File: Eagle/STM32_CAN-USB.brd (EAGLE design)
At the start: 50 x 50 mm, 52 parts, among them IC1 STM32F105RBT, IC2 TJA1055T, IC3 BD9G101G, IC4 LM1117IMPX-3.3, Q1 16MHz, X1 MINI-USB

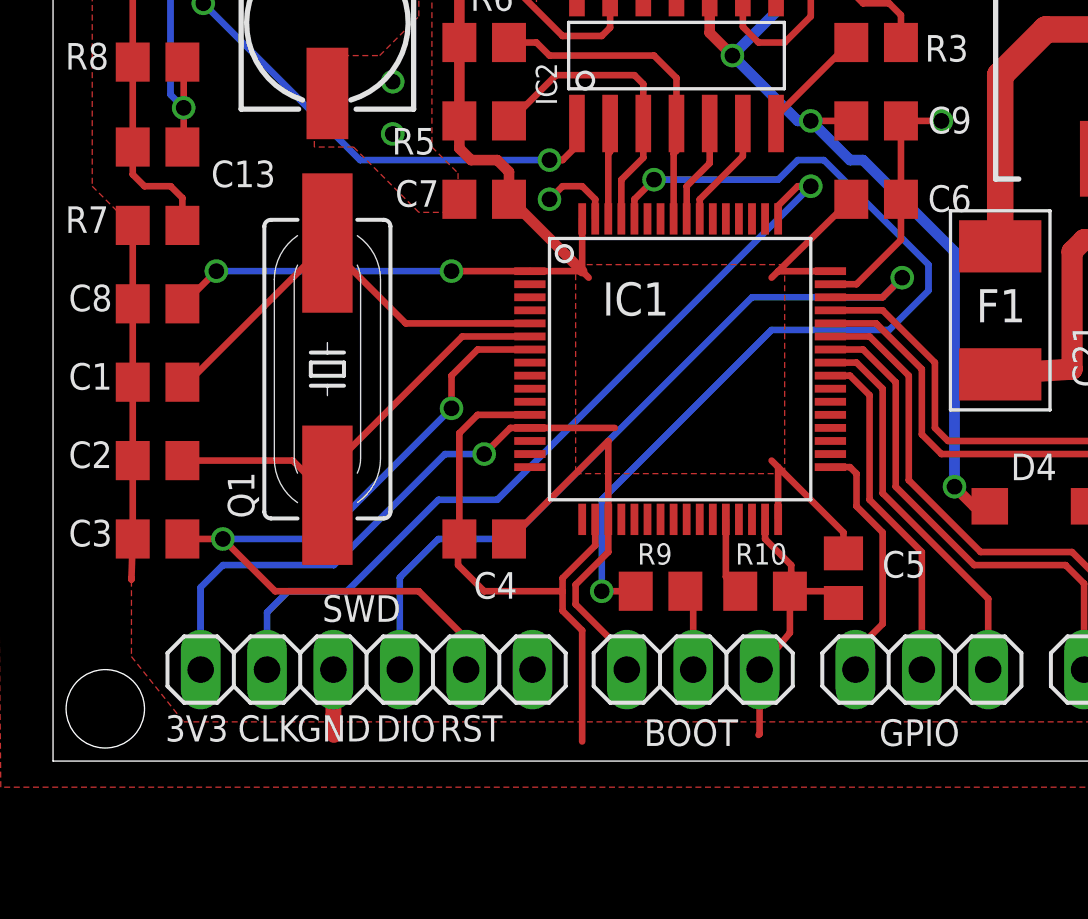
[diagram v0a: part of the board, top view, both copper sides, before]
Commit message: delete boot, edit SWD
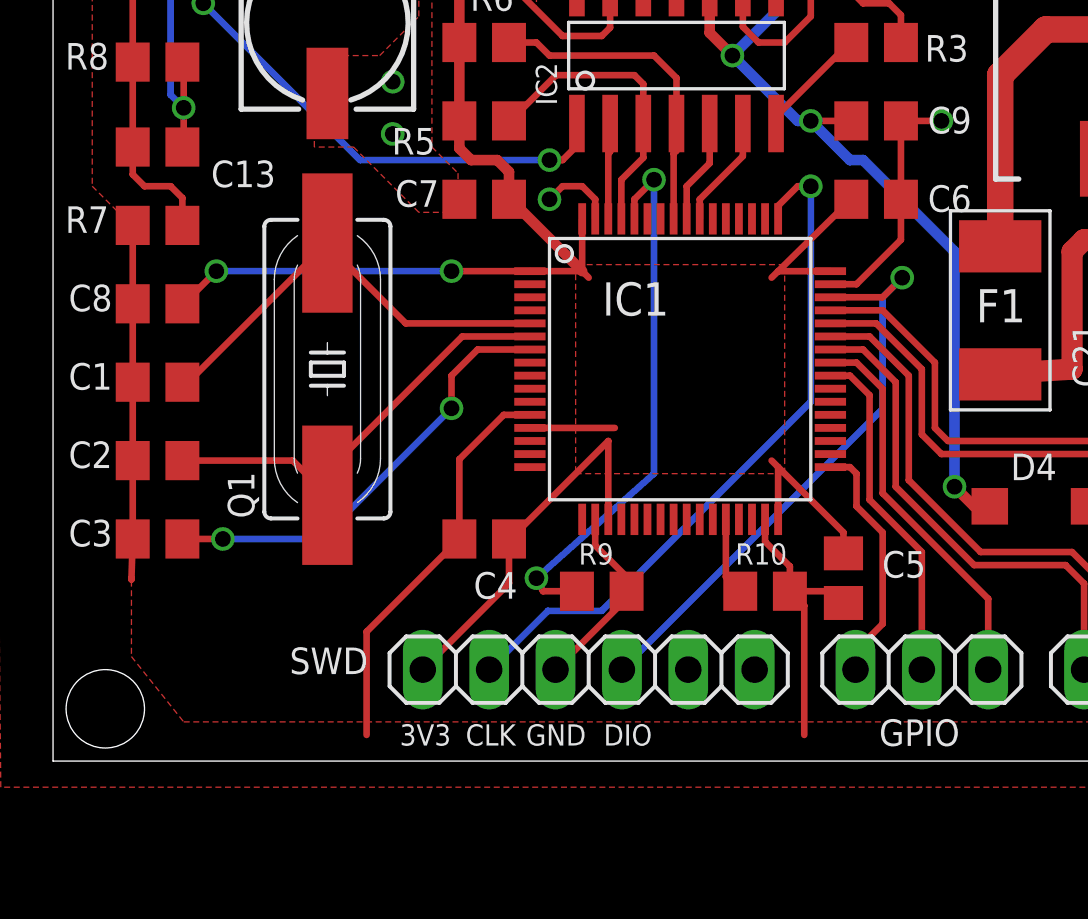
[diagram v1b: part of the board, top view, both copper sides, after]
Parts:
- removed BOOT: (no value), pinhead:1X03
- moved SWD 8.50 mm to (26.5, 8.50)
- moved R9 2.25 mm to (27.0, 11.5)
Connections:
- net BOOT0 renamed N$3
- removed net N$3 (its old number): BOOT.2, R9.2
- net +3V3: no longer BOOT.1
- net GND: now also R9.2; no longer BOOT.3
- net NRST: no longer SWD.5
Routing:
- net +3V3: track 125.0 -> 106.0 mm, vias 6 -> 5
- net N$3: track 35.9 -> 20.9 mm
- net NRST: track 29.1 -> 17.0 mm
- net SWDIO: track 30.6 -> 22.5 mm
- net SWCLK: track 31.8 -> 26.9 mm
- net N$3 (its old number): track 3.12 -> 0.00 mm
- net GND: track 120.1 -> 118.4 mm
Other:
- board text removed: "RST"

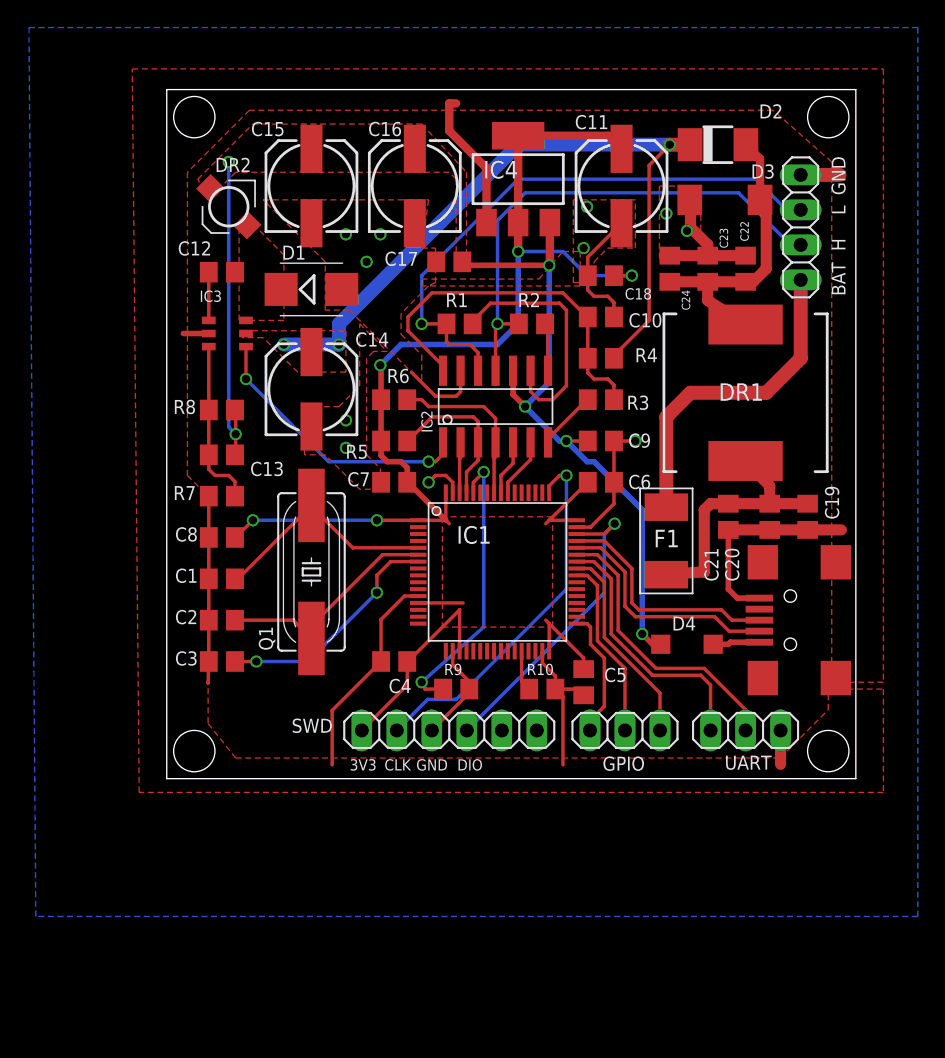
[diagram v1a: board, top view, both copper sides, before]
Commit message: Labels, pin headers optimization
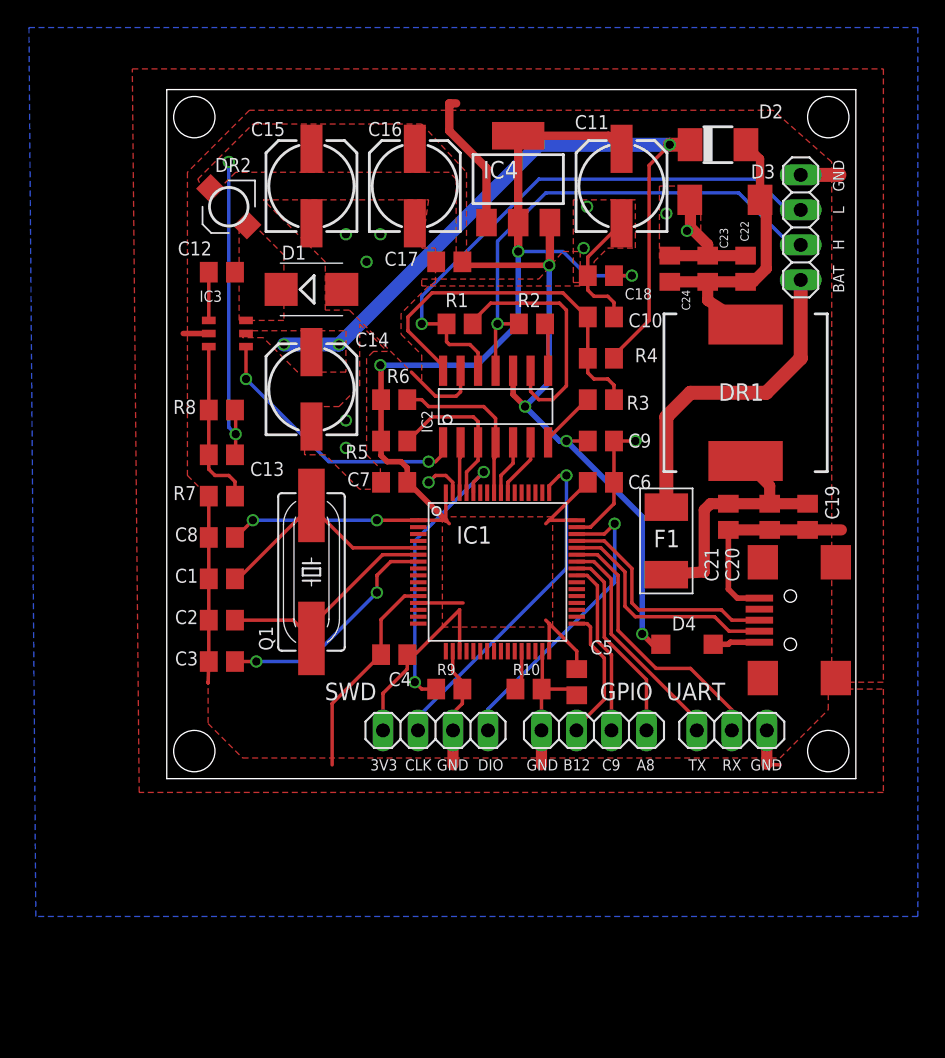
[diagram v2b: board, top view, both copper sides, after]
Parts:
- GPIO: device pinhead:1X03 -> pinhead:1X04
- SWD: device pinhead:1X06 -> pinhead:1X04
- moved GPIO 2.25 mm to (37.0, 8.50)
- moved R10 1.00 mm to (32.2, 11.5)
- moved SWD 1.00 mm to (25.5, 8.50)
- moved UART 1.00 mm to (47.0, 8.50)
- moved C4 0.50 mm to (22.5, 14.0)
- moved C5 0.50 mm to (35.8, 12.0)
- moved R9 0.50 mm to (26.5, 11.5)
- renumbered JP1 to CAN
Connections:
- net GND: now also GPIO.1
- net PA8: now also GPIO.4; no longer GPIO.3
- net PB12: now also GPIO.2; no longer GPIO.1
- net PC9: now also GPIO.3; no longer GPIO.2
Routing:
- net GND: track 118.4 -> 121.2 mm
- net USART1_TX: track 19.1 -> 16.6 mm
- net SWCLK: track 26.9 -> 25.0 mm
- net USART1_RX: track 20.8 -> 19.8 mm
- net CANL: track 41.9 -> 41.0 mm
- net CANH: track 36.9 -> 36.0 mm
- net BAT: track 53.5 -> 52.7 mm
- net SWDIO: track 22.5 -> 21.9 mm
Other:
- board text added: "A8"
- board text added: "B12"
- board text added: "C9"
- board text added: "RX"
- board text added: "TX"

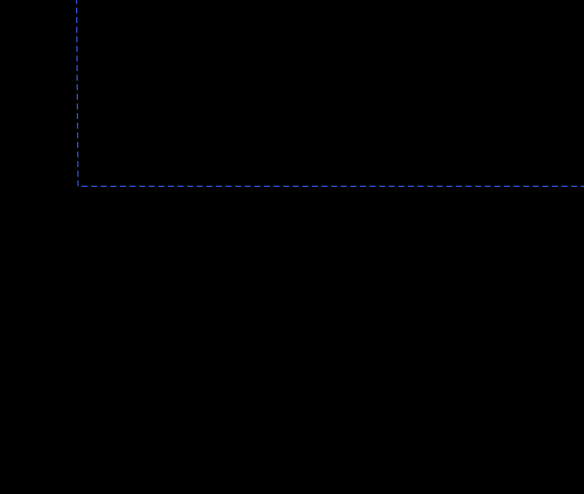
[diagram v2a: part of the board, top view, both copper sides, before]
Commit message: added pull-down resistors on the lines EN and STB
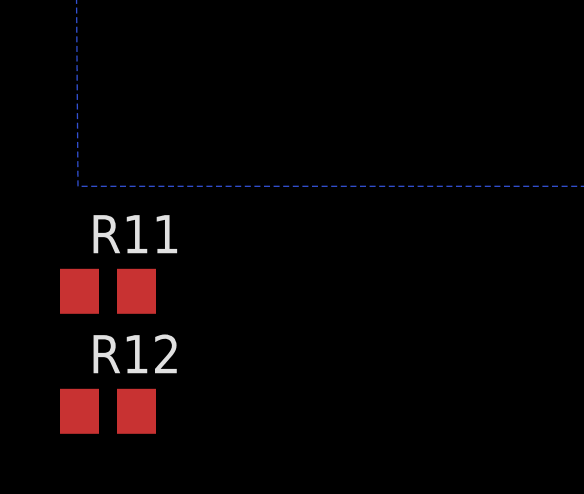
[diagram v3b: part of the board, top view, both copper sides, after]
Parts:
- added R11, R12: 47K, rcl:R0805
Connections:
- net GND: now also R11.1, R12.1
- net N$14: now also R12.2
- net N$6: now also R11.2
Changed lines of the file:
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@@
 <?xml version="1.0" encoding="utf-8"?>
 <!DOCTYPE eagle SYSTEM "eagle.dtd">
-<eagle version="7.4.0">
+<eagle version="7.2.0">
 <drawing>
 <settings>
@@
 <attribute name="VALUE" x="31.92" y="5.325" size="1.27" layer="27"/>
 </element>
+<element name="R11" library="rcl" package="R0805" value="47K" x="-2.5" y="-8.5"/>
+<element name="R12" library="rcl" package="R0805" value="47K" x="-2.5" y="-12.5"/>
 </elements>
 <signals>
@@
 <wire x1="26.77" y1="8.5" x2="26.77" y2="6" width="0.8128" layer="1"/>
 <wire x1="33.19" y1="8.5" x2="33.19" y2="6" width="0.8128" layer="1"/>
+<contactref element="R11" pad="1"/>
+<contactref element="R12" pad="1"/>
+<wire x1="48" y1="42.95" x2="52" y2="48.81" width="0" layer="19" extent="1-1"/>
+<wire x1="43.75" y1="44.75" x2="44" y2="45" width="0" layer="19" extent="1-1"/>
+<wire x1="42.25" y1="46" x2="43.75" y2="44.75" width="0" layer="19" extent="1-1"/>
+<wire x1="39" y1="45.3" x2="42.25" y2="46" width="0" layer="19" extent="1-1"/>
+<wire x1="36.55" y1="41.05" x2="36.55" y2="41.5" width="0" layer="19" extent="1-1"/>
+<wire x1="36.25" y1="43.5" x2="36.55" y2="42.85" width="0" layer="19" extent="1-1"/>
+<wire x1="36.5" y1="46.5" x2="39" y2="45.3" width="0" layer="19" extent="1-1"/>
+<wire x1="29.2" y1="45.35" x2="36.25" y2="43.5" width="0" layer="19" extent="1-1"/>
+<wire x1="25.55" y1="42.5" x2="29.2" y2="45.35" width="0" layer="19" extent="1-1"/>
+<wire x1="24" y1="45.3" x2="25.55" y2="42.5" width="0" layer="19" extent="1-1"/>
+<wire x1="21.5" y1="44.5" x2="24" y2="45.3" width="0" layer="19" extent="1-1"/>
+<wire x1="20.5" y1="42.5" x2="21.5" y2="44.5" width="0" layer="19" extent="1-1"/>
+<wire x1="19" y1="44.5" x2="21.5" y2="44.5" width="0" layer="19" extent="1-1"/>
+<wire x1="16.5" y1="45.3" x2="19" y2="44.5" width="0" layer="19" extent="1-1"/>
+<wire x1="18.7" y1="40.5" x2="20.5" y2="42.5" width="0" layer="19" extent="1-1"/>
+<wire x1="23.75" y1="34.5" x2="18.7" y2="40.5" width="0" layer="19" extent="1-1"/>
+<wire x1="25.5" y1="27" x2="25.5" y2="32.75" width="0" layer="19" extent="1-1"/>
+<wire x1="21.55" y1="26.5" x2="25" y2="26.5" width="0" layer="19" extent="1-1"/>
+<wire x1="19" y1="29" x2="21.5" y2="26.5" width="0" layer="19" extent="1-1"/>
+<wire x1="19" y1="31" x2="19" y2="29" width="0" layer="19" extent="1-1"/>
+<wire x1="16.5" y1="30.55" x2="19" y2="31" width="0" layer="19" extent="1-1"/>
+<wire x1="24.25" y1="18.25" x2="26.75" y2="25.75" width="0" layer="19" extent="1-1"/>
+<wire x1="26.75" y1="14.25" x2="24.25" y2="18.25" width="0" layer="19" extent="1-1"/>
+<wire x1="33.2" y1="11.5" x2="27.95" y2="11.22" width="0" layer="19" extent="1-1"/>
+<wire x1="38.45" y1="29.5" x2="38.45" y2="38.5" width="0" layer="19" extent="1-1"/>
+<wire x1="46.75" y1="23.05" x2="38.45" y2="24.95" width="0" layer="19" extent="1-1"/>
+<wire x1="54.55" y1="20.7" x2="54.95" y2="23.05" width="0" layer="19" extent="1-1"/>
+<wire x1="54.55" y1="12.3" x2="49" y2="18.1" width="0" layer="19" extent="1-1"/>
+<wire x1="49.54" y1="8.5" x2="54.55" y2="12.3" width="0" layer="19" extent="1-1"/>
+<wire x1="9.05" y1="25.5" x2="16.5" y2="30.55" width="0" layer="19" extent="1-1"/>
+<wire x1="9.05" y1="37.3" x2="16.5" y2="30.55" width="0" layer="19" extent="1-1"/>
+<wire x1="-3.45" y1="-8.5" x2="9" y2="11.95" width="0" layer="19" extent="1-1"/>
+<wire x1="-3.45" y1="-12.5" x2="-3.45" y2="-8.5" width="0" layer="19" extent="1-1"/>
 </signal>
 <signal name="+3V3">
@@
 <wire x1="30.75" y1="25.75" x2="30.75" y2="26.5" width="0.254" layer="1"/>
 <wire x1="30.75" y1="26.5" x2="32.4" y2="28.15" width="0.254" layer="1"/>
+<contactref element="R12" pad="2"/>
+<wire x1="-1.55" y1="-12.5" x2="30.75" y2="25.75" width="0" layer="19" extent="1-1"/>
 </signal>
 <signal name="N$6">
@@
 <wire x1="30.25" y1="25.75" x2="30.25" y2="27" width="0.254" layer="1"/>
 <wire x1="30.25" y1="27" x2="31.13" y2="27.88" width="0.254" layer="1"/>
+<contactref element="R11" pad="2"/>
+<wire x1="-1.55" y1="-8.5" x2="30.25" y2="25.75" width="0" layer="19" extent="1-1"/>
 </signal>
 <signal name="N$15">
